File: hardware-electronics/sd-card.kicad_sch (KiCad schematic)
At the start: 40 parts, among them J5 Micro_SD_Card_Det_Hirose_DM3AT, J8 TC2030-IDC-NL, U6 24AA04T-I_OT, U9 USB2244-AEZG-06, Y3 ECS-240-10-47-CKM-TR

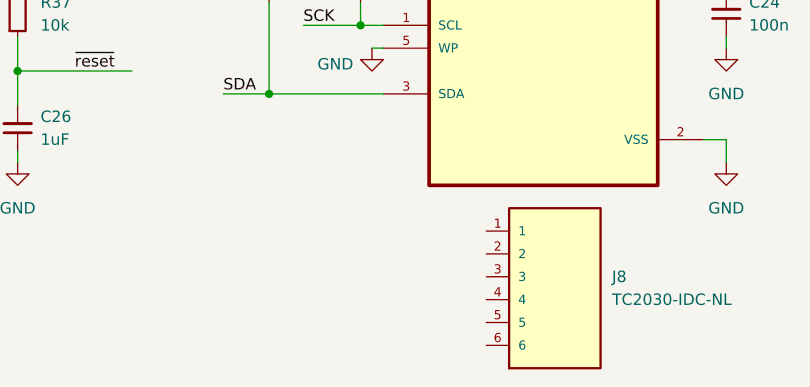
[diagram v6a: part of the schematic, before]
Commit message: [#26] Add programing interface for I2c devices
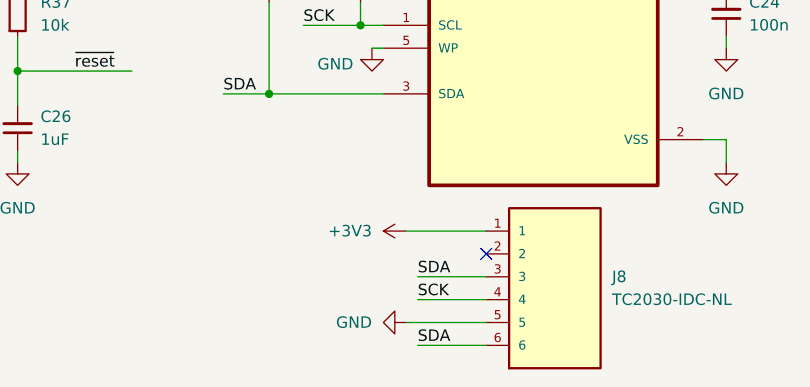
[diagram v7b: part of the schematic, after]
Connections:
- net +3V3: now also J8.1
- net GND: now also J8.5
- net SCK: now also J8.4
- net SDA: now also J8.3, J8.6
- no-connect marks 4 -> 5
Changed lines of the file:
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@@
 	)
 	(no_connect
+		(at 135.89 186.69)
+	)
+	(no_connect
 		(at 142.24 81.28)
 	)
@@
 	(wire
 		(pts
+			(xy 128.27 191.77) (xy 135.89 191.77)
+		)
+		(stroke
+			(width 0)
+			(type default)
+		)
+	)
+	(wire
+		(pts
 			(xy 60.96 95.25) (xy 68.58 95.25)
 		)
@@
 	(wire
 		(pts
+			(xy 127 194.31) (xy 135.89 194.31)
+		)
+		(stroke
+			(width 0)
+			(type default)
+		)
+	)
+	(wire
+		(pts
 			(xy 123.19 68.58) (xy 123.19 91.44)
 		)
@@
 	(wire
 		(pts
+			(xy 128.27 196.85) (xy 135.89 196.85)
+		)
+		(stroke
+			(width 0)
+			(type default)
+		)
+	)
+	(wire
+		(pts
 			(xy 123.19 116.84) (xy 123.19 99.06)
 		)
@@
 	(wire
 		(pts
+			(xy 128.27 189.23) (xy 135.89 189.23)
+		)
+		(stroke
+			(width 0)
+			(type default)
+		)
+	)
+	(wire
+		(pts
 			(xy 62.23 180.34) (xy 62.23 177.8)
 		)
@@
 	(wire
 		(pts
+			(xy 127 184.15) (xy 135.89 184.15)
+		)
+		(stroke
+			(width 0)
+			(type default)
+		)
+	)
+	(wire
+		(pts
 			(xy 34.29 157.48) (xy 34.29 160.02)
 		)
@@
 		)
 	)
+	(label "SDA"
+		(at 128.27 189.23 0)
+		(fields_autoplaced yes)
+		(effects
+			(font
+				(size 1.27 1.27)
+			)
+			(justify left bottom)
+		)
+	)
 	(label "XTAL1"
 		(at 135.89 67.31 0)
@@
 		)
 	)
+	(label "SDA"
+		(at 128.27 196.85 0)
+		(fields_autoplaced yes)
+		(effects
+			(font
+				(size 1.27 1.27)
+			)
+			(justify left bottom)
+		)
+	)
 	(label "uSD.D0"
 		(at 68.58 82.55 180)
@@
 		)
 	)
+	(label "SCK"
+		(at 128.27 191.77 0)
+		(fields_autoplaced yes)
+		(effects
+			(font
+				(size 1.27 1.27)
+			)
+			(justify left bottom)
+		)
+	)
 	(label "uSD.D3"
 		(at 90.17 78.74 0)
@@
 	)
 	(symbol
+		(lib_id "power:GND")
+		(at 127 194.31 270)
+		(unit 1)
+		(exclude_from_sim no)
+		(in_bom yes)
+		(on_board yes)
+		(dnp no)
+		(fields_autoplaced yes)
+		(property "Reference" "#PWR0174"
+			(at 120.65 194.31 0)
+			(effects
+				(font
+					(size 1.27 1.27)
+				)
+				(hide yes)
+			)
+		)
+		(property "Value" "GND"
+			(at 123.19 194.3099 90)
+			(effects
+				(font
+					(size 1.27 1.27)
+				)
+				(justify right)
+			)
+		)
+		(property "Footprint" ""
+			(at 127 194.31 0)
+			(effects
+				(font
+					(size 1.27 1.27)
+				)
+				(hide yes)
+			)
+		)
+		(property "Datasheet" ""
+			(at 127 194.31 0)
+			(effects
+				(font
+					(size 1.27 1.27)
+				)
+				(hide yes)
+			)
+		)
+		(property "Description" "Power symbol creates a global label with name \"GND\" , ground"
+			(at 127 194.31 0)
+			(effects
+				(font
+					(size 1.27 1.27)
+				)
+				(hide yes)
+			)
+		)
+		(pin "1"
+		)
+		(instances
+			(project "M2SmartHome"
+				(path "/da663dec-9e91-4003-a791-431d460ad63c/2a53ffe2-5715-44b3-b464-b3185e5be86d"
+					(reference "#PWR0174")
+					(unit 1)
+				)
+			)
+		)
+	)
+	(symbol
 		(lib_id "power:+3V3")
 		(at 87.63 49.53 0)
@@
 					(unit 1)
 				)
+			)
+		)
+	)
+	(symbol
+		(lib_id "power:+3V3")
+		(at 127 184.15 90)
+		(unit 1)
+		(exclude_from_sim no)
+		(in_bom yes)
+		(on_board yes)
+		(dnp no)
+		(fields_autoplaced yes)
+		(property "Reference" "#PWR0173"
+			(at 130.81 184.15 0)
+			(effects
+				(font
+					(size 1.27 1.27)
+				)
+				(hide yes)
+			)
+		)
+		(property "Value" "+3V3"
+			(at 123.19 184.1499 90)
+			(effects
+				(font
+					(size 1.27 1.27)
+				)
+				(justify left)
+			)
+		)
+		(property "Footprint" ""
+			(at 127 184.15 0)
+			(effects
+				(font
+					(size 1.27 1.27)
+				)
+				(hide yes)
+			)
+		)
+		(property "Datasheet" ""
+			(at 127 184.15 0)
+			(effects
+				(font
+					(size 1.27 1.27)
+				)
+				(hide yes)
+			)
+		)
+		(property "Description" "Power symbol creates a global label with name \"+3V3\""
+			(at 127 184.15 0)
+			(effects
+				(font
+					(size 1.27 1.27)
+				)
+				(hide yes)
+			)
+		)
+		(pin "1"
+		)
+		(instances
+			(project "M2SmartHome"
+				(path "/da663dec-9e91-4003-a791-431d460ad63c/2a53ffe2-5715-44b3-b464-b3185e5be86d"
+					(reference "#PWR0173")
+					(unit 1)
+				)

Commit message: [#26] Correct MPN GRM155R61A104KA01D
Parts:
- C24, C27, C29, C31, C33, C39: Author Your Name -> Lukasz Nowarkiewicz; MPN GRM155R61A104KE01D -> GRM155R61A104KA01D
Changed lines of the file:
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@@
 			)
 		)
-		(property "MPN" "GRM155R61A104KE01D"
+		(property "MPN" "GRM155R61A104KA01D"
 			(at 245.11 78.74 0)
 			(effects
@@
 			)
 		)
-		(property "Author" "Your Name"
+		(property "Author" "Lukasz Nowarkiewicz"
 			(at 252.73 78.74 0)
 			(effects
@@
 			)
 		)
-		(property "MPN" "GRM155R61A104KE01D"
+		(property "MPN" "GRM155R61A104KA01D"
 			(at 227.33 78.74 0)
 			(effects
@@
 			)
 		)
-		(property "Author" "Your Name"
+		(property "Author" "Lukasz Nowarkiewicz"
 			(at 234.95 78.74 0)
 			(effects
@@
 			)
 		)
-		(property "MPN" "GRM155R61A104KE01D"
+		(property "MPN" "GRM155R61A104KA01D"
 			(at 123.19 87.63 0)
 			(effects
@@
 			)
 		)
-		(property "Author" "Your Name"
+		(property "Author" "Lukasz Nowarkiewicz"
 			(at 130.81 87.63 0)
 			(effects
@@
 			)
 		)
-		(property "MPN" "GRM155R61A104KE01D"
+		(property "MPN" "GRM155R61A104KA01D"
 			(at 267.97 74.93 0)
 			(effects
@@
 			)
 		)
-		(property "Author" "Your Name"
+		(property "Author" "Lukasz Nowarkiewicz"
 			(at 275.59 74.93 0)
 			(effects
@@
 			)
 		)
-		(property "MPN" "GRM155R61A104KE01D"
+		(property "MPN" "GRM155R61A104KA01D"
 			(at 180.34 142.24 0)
 			(effects
@@
 			)
 		)
-		(property "Author" "Your Name"
+		(property "Author" "Lukasz Nowarkiewicz"
 			(at 187.96 142.24 0)
 			(effects
@@
 			)
 		)
-		(property "MPN" "GRM155R61A104KE01D"
+		(property "MPN" "GRM155R61A104KA01D"
 			(at 201.93 86.36 0)
 			(effects
@@
 			)
 		)
-		(property "Author" "Your Name"
+		(property "Author" "Lukasz Nowarkiewicz"
 			(at 209.55 86.36 0)
 			(effects
